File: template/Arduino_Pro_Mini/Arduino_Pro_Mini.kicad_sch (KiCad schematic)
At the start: 5 parts, among them P1 Digital, P2 COM, P3 ADC, P4 Analog, P5 ADC

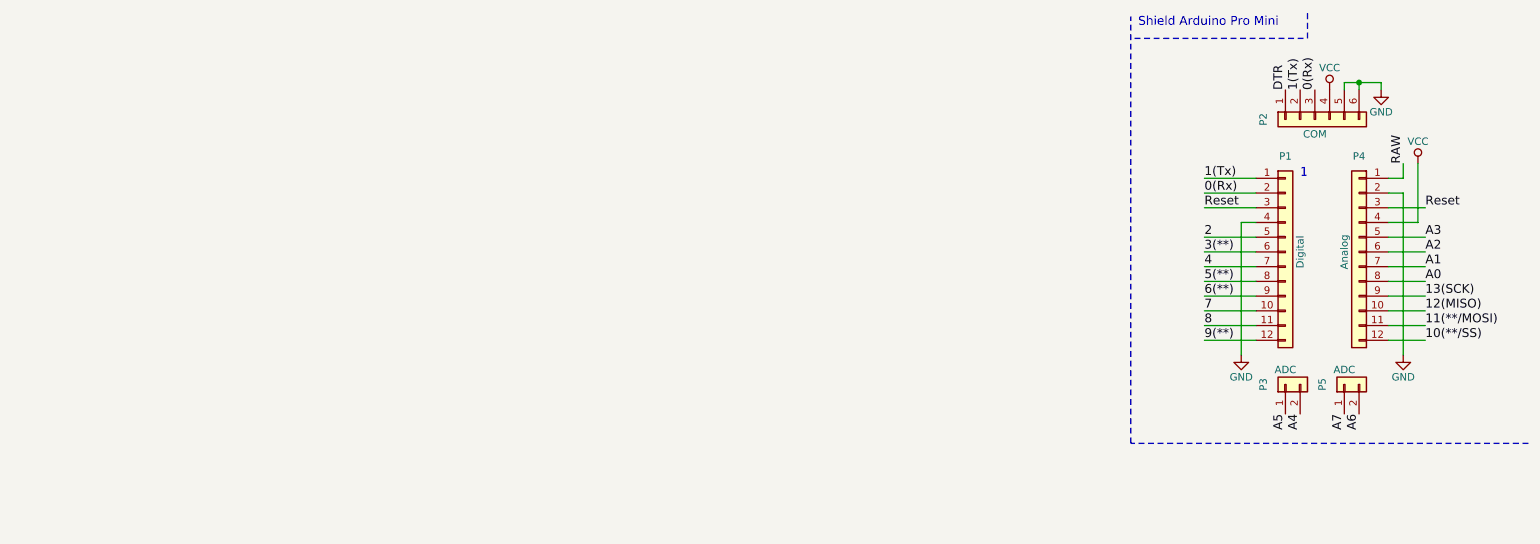
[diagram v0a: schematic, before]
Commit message: fix: change original libs; add: new components
- Fix LIS3DH pins positions;
- Add ATmega164P symbol;
- Add 3D model to the L_Wuerth_HCM-7050;
- Add parameters for R_RES (Assembly...).
- Add parameters for R_RES and C_CAP;
- Fix SOIC-8 package 3D model;
- Add new parameters for many symbols;
- Change text height from 70 mil to 50 mil;
- Add solder mask expansion for 2-contact jumpers;
- Change thermopad vias of QFN-20-1EP_3x3mm_P0.45mm_EP1.6x1.6mm_ThermalVias;
- Add D_SMAF footprint;
- Fillet silk for C_1206;
-Rectangle silk for R_1206;
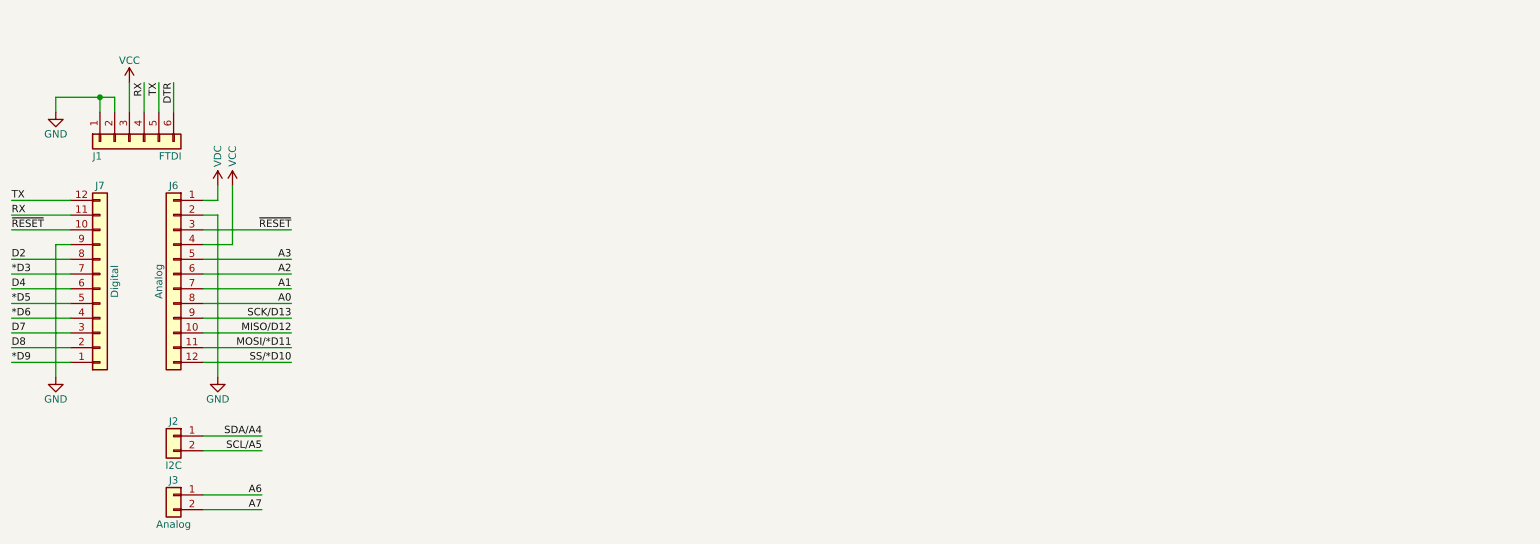
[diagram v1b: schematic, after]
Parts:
- removed P1: Digital, Socket_Arduino_Pro_Mini:Socket_Strip_Arduino_1x12, symbol Connector_Generic:Conn_01x12
- removed P2: COM, Socket_Arduino_Pro_Mini:Socket_Strip_Arduino_1x06, symbol Connector_Generic:Conn_01x06
- removed P3, P5: ADC, Socket_Arduino_Pro_Mini:Socket_Strip_Arduino_1x02, symbol Connector_Generic:Conn_01x02
- removed P4: Analog, Socket_Arduino_Pro_Mini:Socket_Strip_Arduino_1x12, symbol Connector_Generic:Conn_01x12
- added J1: FTDI, Connector_PinHeader_2.54mm:PinHeader_1x06_P2.54mm_Horizontal, symbol Connector_Generic:Conn_01x06
- added J2: I2C, Connector_PinHeader_2.54mm:PinHeader_1x02_P2.54mm_Vertical, symbol Connector_Generic:Conn_01x02
- added J3: Analog, Connector_PinHeader_2.54mm:PinHeader_1x02_P2.54mm_Vertical, symbol Connector_Generic:Conn_01x02
- added J6: Analog, Connector_PinHeader_2.54mm:PinHeader_1x12_P2.54mm_Vertical, symbol Connector_Generic:Conn_01x12
- added J7: Digital, Connector_PinHeader_2.54mm:PinHeader_1x12_P2.54mm_Vertical, symbol Connector_Generic:Conn_01x12
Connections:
- net A0: now also J6.8 (Pin_8)
- net A1: now also J6.7 (Pin_7)
- net A2: now also J6.6 (Pin_6)
- net A3: now also J6.5 (Pin_5)
- net A6: now also J3.1 (Pin_1)
- net A7: now also J3.2 (Pin_2)
- net DTR: now also J1.6 (Pin_6)
- net GND: now also J1.1 (Pin_1), J1.2 (Pin_2), J6.2 (Pin_2), J7.9 (Pin_9)
- net VCC: now also J1.3 (Pin_3), J6.4 (Pin_4)
- new net *D3: J7.7 (Pin_7)
- new net *D5: J7.5 (Pin_5)
- new net *D6: J7.4 (Pin_4)
- new net *D9: J7.1 (Pin_1)
- new net D2: J7.8 (Pin_8)
- new net D4: J7.6 (Pin_6)
- new net D7: J7.3 (Pin_3)
- new net D8: J7.2 (Pin_2)
- new net MISO/D12: J6.10 (Pin_10)
- new net MOSI/*D11: J6.11 (Pin_11)
- new net RX: J1.4 (Pin_4), J7.11 (Pin_11)
- new net SCK/D13: J6.9 (Pin_9)
- new net SCL/A5: J2.2 (Pin_2)
- new net SDA/A4: J2.1 (Pin_1)
- new net SS/*D10: J6.12 (Pin_12)
- new net TX: J1.5 (Pin_5), J7.12 (Pin_12)
- new net VDC: J6.1 (Pin_1)
- new net ~{RESET}: J6.3 (Pin_3), J7.10 (Pin_10)
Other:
- note removed: "1"
- note removed: "Shield Arduino Pro Mini"
